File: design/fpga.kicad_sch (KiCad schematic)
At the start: 80 parts, among them J7 DEBUG_FPGA_GPIO, J8 DIGILENT_JTAG_HS2_01X06, SW1 RST, SW2 PROG, U13 XC7S15-FTGB196, U14 IS25LP064A-JKx

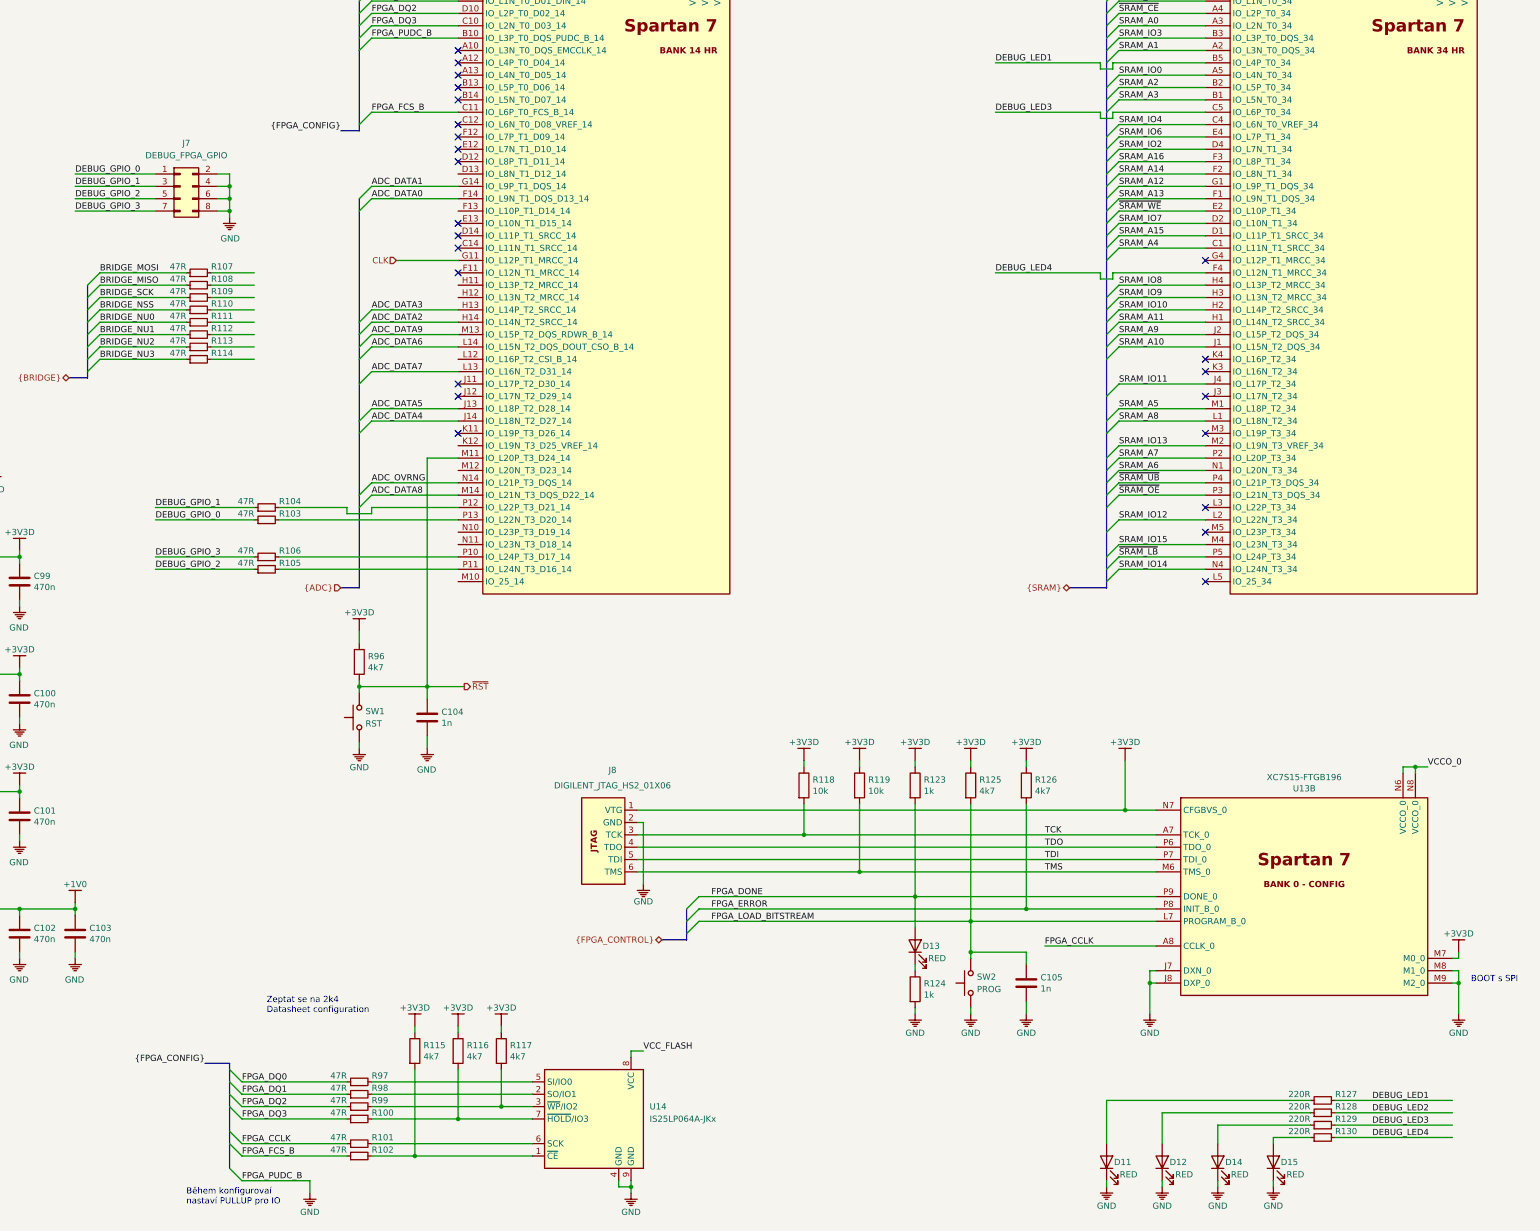
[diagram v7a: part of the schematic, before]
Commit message: Added MCU LED layout
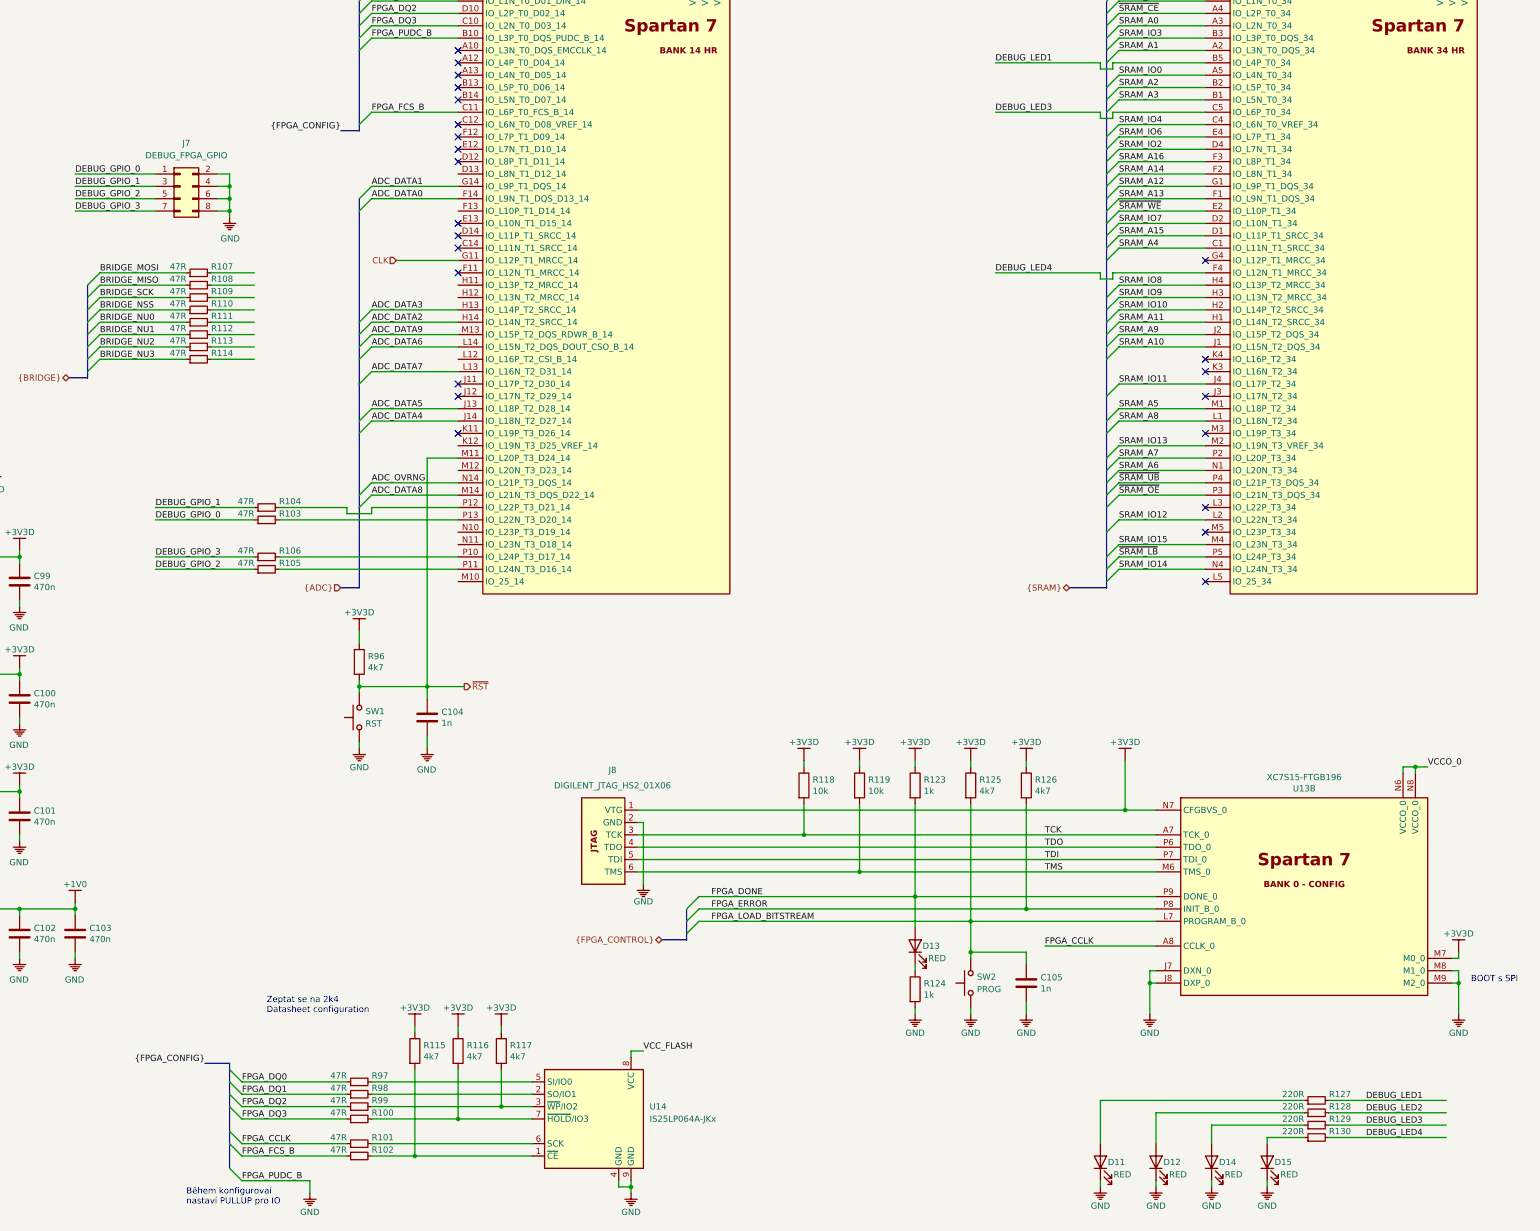
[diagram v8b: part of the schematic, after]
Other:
- moved on the sheet: D11, D12, D14, D15, R127, R128, R129, R130
